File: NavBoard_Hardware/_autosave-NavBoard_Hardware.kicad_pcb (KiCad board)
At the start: 2 copper layers, 124.5 x 79.2 mm, 46 parts, among them J1 6 Pin Molex Micro-Fit, J2 Raspberry Pi - Header Socket, U1 OKI-5V, U2 BHI160B, U3 ICM-20608-G, U4 OKI-3V3

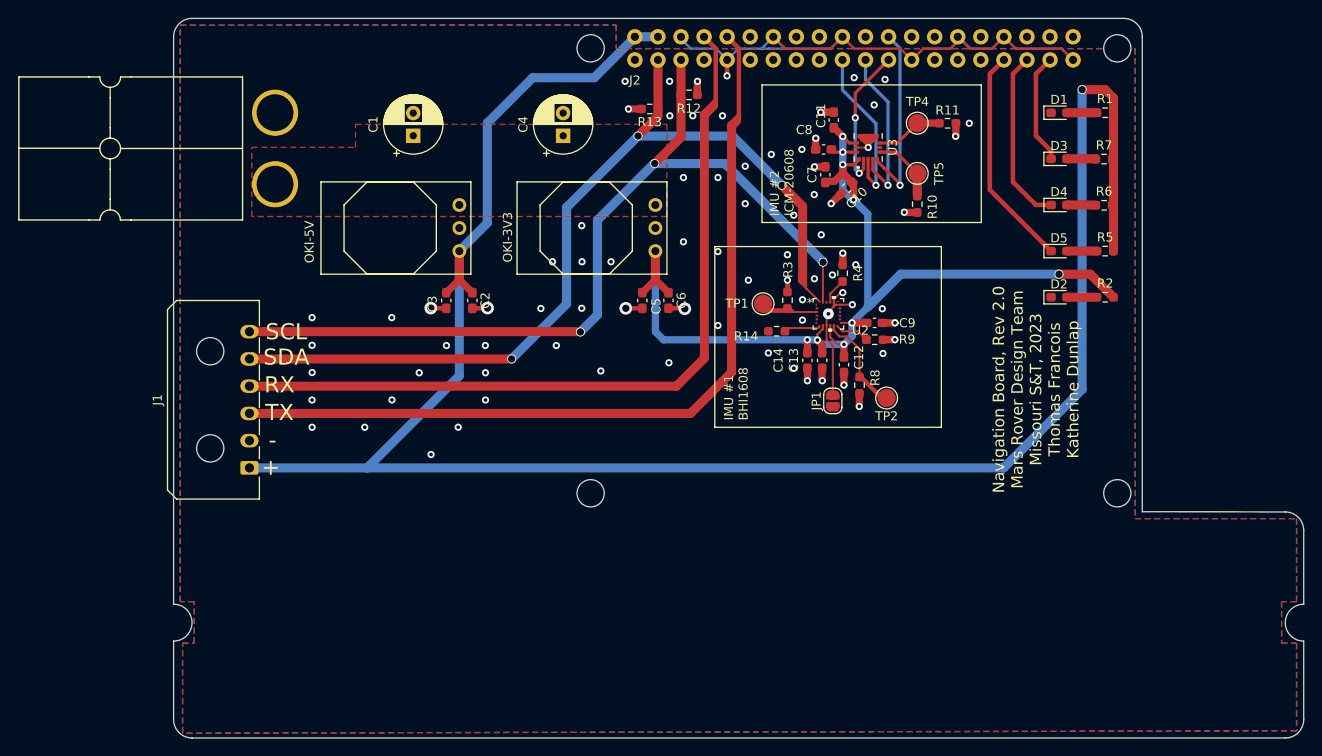
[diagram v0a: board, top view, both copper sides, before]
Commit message: Adjusted LED silkscreen
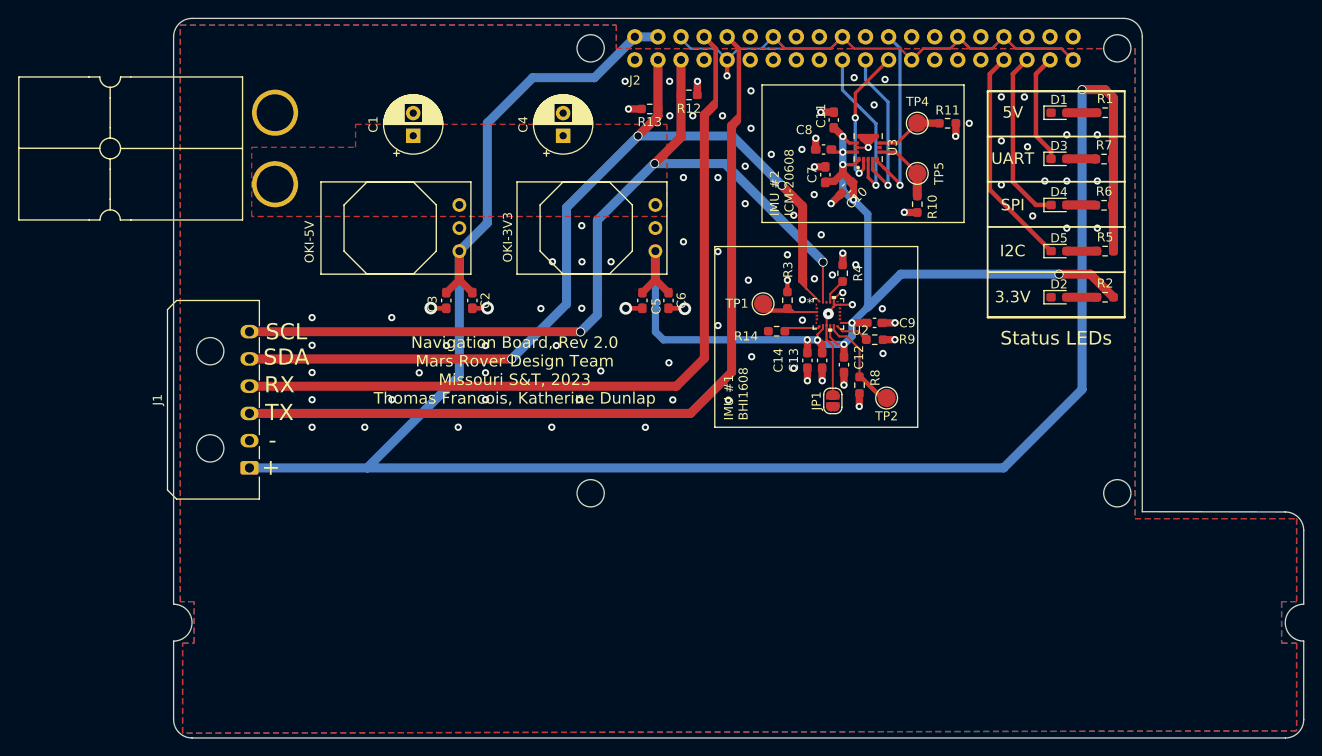
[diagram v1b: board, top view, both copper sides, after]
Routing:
- net /IMU #1 - BHI160B/I2C_ADR: track 0.00 -> 7.96 mm
- net GND: track 138.4 -> 130.4 mm, vias 81 -> 100
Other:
- board text added: "3.3V"
- board text added: "5V"
- board text added: "I2C"
- board text added: "Navigation Board, Rev 2.0 Mars Rover Design Team Missouri S&T, 2023 Thomas Francois, Katherine Dunlap"
- board text added: "SPI"
- board text added: "Status LEDs"
- board text added: "UART"
- board text removed: "Navigation Board, Rev 2.0 Mars Rover Design Team Missouri S&T, 2023 Thomas Francois Katherine Dunlap"
